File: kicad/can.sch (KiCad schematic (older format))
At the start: 5 parts

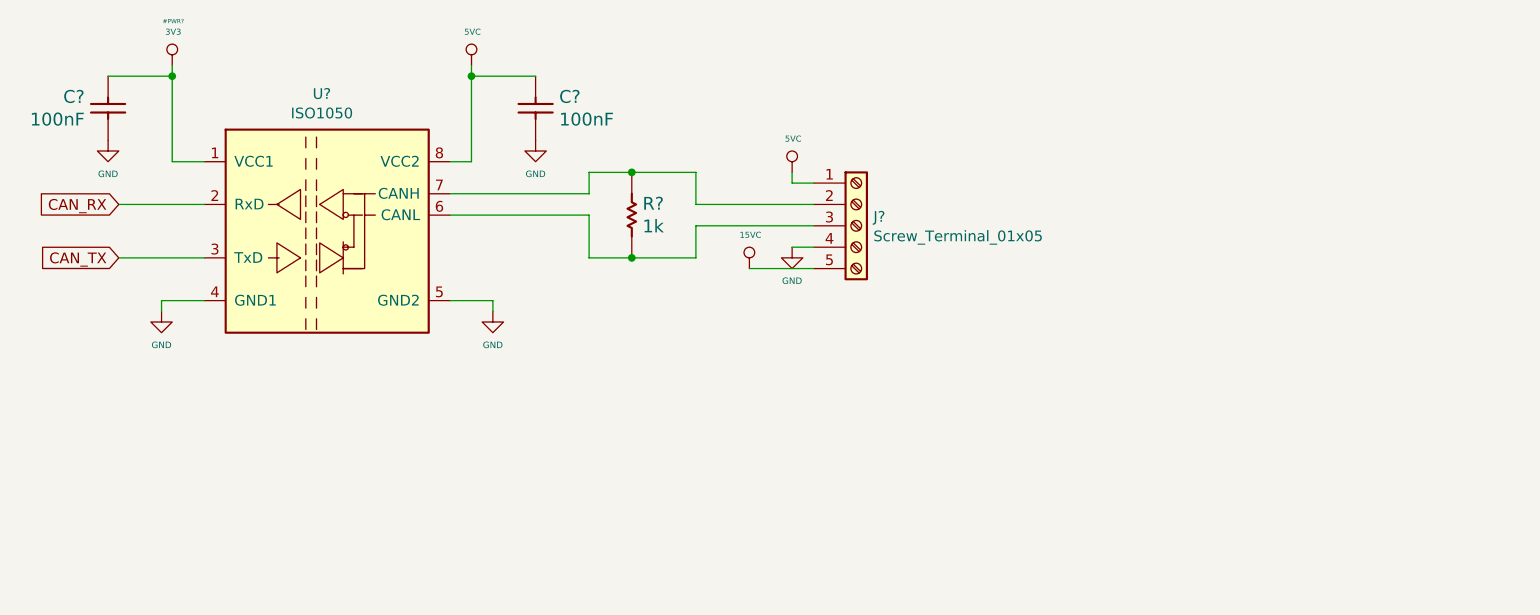
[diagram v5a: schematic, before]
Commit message: I've added LCD UI interfase, EQEP and finish ENDAT
I think I have almos all the interfases ready, I'm begining the
verigication process and then the part definig
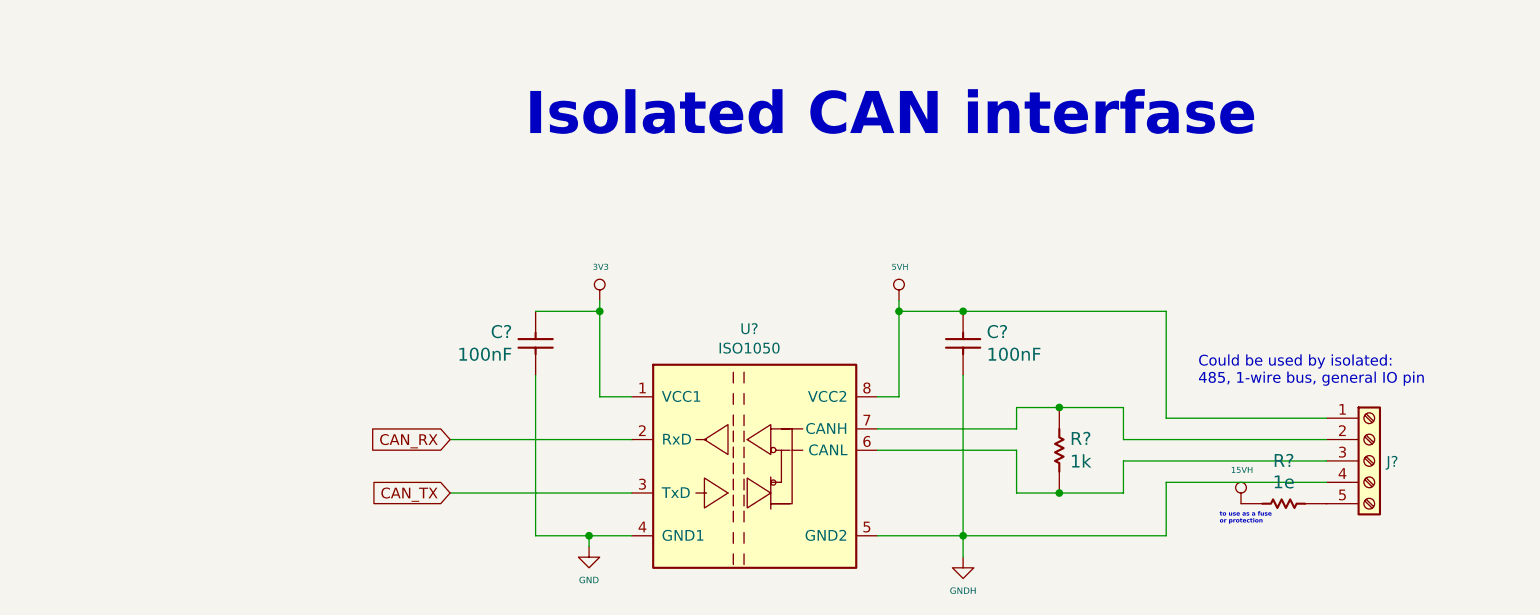
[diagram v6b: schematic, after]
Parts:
- removed J?: Screw_Terminal_01x05, symbol Connector:Screw_Terminal_01x05
- added J?: Screw_Terminal_01x05, symbol Connector:Screw_Terminal_01x05
- added R?: 1e, symbol servo:Resistor
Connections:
- net GND: no longer C?.1, U?.5 (GND2)
- net at R?.1, U?.6 (CANL): now also J?.3 (Pin_3)
- net at R?.2, U?.7 (CANH): now also J?.2 (Pin_2)
- net 5VC renamed 5VH
- net 5VH: now also J?.1 (Pin_1)
- new net: J?.5 (Pin_5), R?.1
- new net 15VH: R?.2
- new net GNDH: C?.1, J?.4 (Pin_4), U?.5 (GND2)
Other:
- note added: "Could be used by isolated: \n485, 1-wire bus, general IO pin"
- note added: "Isolated CAN interfase"
- note added: "to use as a fuse \nor protection"
- moved on the sheet: C?, R?, U?

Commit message: added 4 push buttons and more gpios on LCD connector
just to have more UI options. With those I'd manage graphics LCD plus 4
buttons, and charaveter LCD. or the embedded EVE graphic LCD
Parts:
- gave numbers to parts that had none: 6
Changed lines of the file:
@@
 $EndDescr
 $Comp
-L servo:ISO1050 U?
+L servo:ISO1050 U1301
 U 1 1 5E217E51
 P 4850 3050
-F 0 "U?" H 4850 3817 50  0000 C CNN
+F 0 "U1301" H 4850 3817 50  0000 C CNN
 F 1 "ISO1050" H 4850 3726 50  0000 C CNN
 F 2 "Package_SO:SOIC-16W_7.5x10.3mm_P1.27mm" H 4850 2350 50  0001 C CNN
@@
 $EndComp
 $Comp
-L servo:Resistor R?
+L servo:Resistor R1301
 U 1 1 5E21D81F
 P 6300 2850
-F 0 "R?" V 6353 2800 60  0000 R CNN
+F 0 "R1301" V 6353 2800 60  0000 R CNN
 F 1 "1k" V 6247 2800 60  0000 R CNN
 F 2 "" H 6300 2850 60  0000 C CNN
@@
 AR Path="/5DE3DF56/5E21DD67" Ref="#PWR?"  Part="1"
 AR Path="/5E1BAEAA/5E21DD67" Ref="#PWR?"  Part="1"
-AR Path="/5E21534F/5E21DD67" Ref="#PWR?"  Part="1"
-F 0 "#PWR?" H 4155 2357 20  0001 C CNN
+AR Path="/5E21534F/5E21DD67" Ref="#PWR0239"  Part="1"
+F 0 "#PWR0239" H 4155 2357 20  0001 C CNN
 F 1 "3V3" H 4155 2307 28  0000 C CNN
 F 2 "" H 4150 2150 50  0001 C CNN
@@
 AR Path="/5DE3DF56/5E21DD6E" Ref="C?"  Part="1"
 AR Path="/5E1BAEAA/5E21DD6E" Ref="C?"  Part="1"
-AR Path="/5E21534F/5E21DD6E" Ref="C?"  Part="1"
-F 0 "C?" V 5847 2410 60  0000 L CNN
+AR Path="/5E21534F/5E21DD6E" Ref="C1302"  Part="1"
+F 0 "C1302" V 5847 2410 60  0000 L CNN
 F 1 "100nF" V 5953 2410 60  0000 L CNN
 F 2 "" H 5850 2300 60  0000 C CNN
@@
 AR Path="/5DE3DF56/5E21DD7B" Ref="C?"  Part="1"
 AR Path="/5E1BAEAA/5E21DD7B" Ref="C?"  Part="1"
-AR Path="/5E21534F/5E21DD7B" Ref="C?"  Part="1"
-F 0 "C?" V 3847 2191 60  0000 R CNN
+AR Path="/5E21534F/5E21DD7B" Ref="C1301"  Part="1"
+F 0 "C1301" V 3847 2191 60  0000 R CNN
 F 1 "100nF" V 3953 2191 60  0000 R CNN
 F 2 "" H 3850 2300 60  0000 C CNN
@@
 AR Path="/5DE3DF56/5E221639" Ref="#PWR?"  Part="1"
 AR Path="/5E1BAEAA/5E221639" Ref="#PWR?"  Part="1"
-AR Path="/5E21534F/5E221639" Ref="#PWR?"  Part="1"
-F 0 "#PWR?" H 4100 3050 30  0001 C CNN
+AR Path="/5E21534F/5E221639" Ref="#PWR0240"  Part="1"
+F 0 "#PWR0240" H 4100 3050 30  0001 C CNN
 F 1 "GND" H 4100 3142 30  0000 C CNN
 F 2 "" H 4100 3300 50  0001 C CNN
@@
 AR Path="/5DE49152/5E32E6BC" Ref="#PWR?"  Part="1"
 AR Path="/5E1BAEAA/5E32E6BC" Ref="#PWR?"  Part="1"
-AR Path="/5E21534F/5E32E6BC" Ref="#PWR?"  Part="1"
-F 0 "#PWR?" H 5550 1950 20  0001 C CNN
+AR Path="/5E21534F/5E32E6BC" Ref="#PWR0241"  Part="1"
+F 0 "#PWR0241" H 5550 1950 20  0001 C CNN
 F 1 "5VH" H 5555 2307 28  0000 C CNN
 F 2 "" H 5550 2150 50  0001 C CNN
@@
 AR Path="/5E1BAEAA/5E33F739" Ref="R?"  Part="1"
 AR Path="/5DE49152/5E33F739" Ref="R?"  Part="1"
-AR Path="/5E21534F/5E33F739" Ref="R?"  Part="1"
-F 0 "R?" H 7350 2900 60  0000 C CNN
+AR Path="/5E21534F/5E33F739" Ref="R1302"  Part="1"
+F 0 "R1302" H 7350 2900 60  0000 C CNN
 F 1 "1e" H 7350 3000 60  0000 C CNN
 F 2 "" H 7350 3100 60  0000 C CNN
@@
 P 7750 2900
 AR Path="/5E1BAEAA/5E33F741" Ref="J?"  Part="1"
-AR Path="/5E21534F/5E33F741" Ref="J?"  Part="1"
-F 0 "J?" H 7830 2896 50  0000 L CNN
+AR Path="/5E21534F/5E33F741" Ref="J1301"  Part="1"
+F 0 "J1301" H 7830 2896 50  0000 L CNN
 F 1 "Screw_Terminal_01x05" H 7830 2851 50  0001 L CNN
 F 2 "" H 7750 2900 50  0001 C CNN
@@
 AR Path="/5DE3DF56/5E33F748" Ref="#PWR?"  Part="1"
 AR Path="/5E1BAEAA/5E33F748" Ref="#PWR?"  Part="1"
-AR Path="/5E21534F/5E33F748" Ref="#PWR?"  Part="1"
-F 0 "#PWR?" H 7150 2900 20  0001 C CNN
+AR Path="/5E21534F/5E33F748" Ref="#PWR0242"  Part="1"
+F 0 "#PWR0242" H 7150 2900 20  0001 C CNN
 F 1 "15VH" H 7155 3257 28  0000 C CNN
 F 2 "" H 7150 3100 50  0001 C CNN
@@
 AR Path="/5DE49152/5E3402F1" Ref="#PWR?"  Part="1"
 AR Path="/5E1BAEAA/5E3402F1" Ref="#PWR?"  Part="1"
-F 0 "#PWR?" H 5850 3100 30  0001 C CNN
+AR Path="/5E21534F/5E3402F1" Ref="#PWR0243"  Part="1"
+F 0 "#PWR0243" H 5850 3100 30  0001 C CNN
 F 1 "GNDH" H 5850 3192 30  0000 C CNN
 F 2 "" H 5850 3350 50  0001 C CNN
